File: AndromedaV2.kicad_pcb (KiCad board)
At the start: 2 copper layers, 100 x 65 mm, 94 parts, among them J1 USB_MINIB, J10 TEST_1P, J11 TEST_1P, J12 Micro_SD_Card, J13 TEST_1P, J14 TEST_1P, J15 TEST_1P, J16 TEST_1P, J17 TEST_1P, J18 GPS, J19 Radio, J2 TEST_1P, J20 Recovery, J21 Propulsion, J22 Tank Pressure, J23 Low Pressure, J24 Conn_01x06, J25 Battery, J26 Launch Systems, J27 SD, J3 TEST_1P, J4 TEST_1P, J5 TEST_1P, J6 TEST_1P, J7 TEST_1P, J8 TEST_1P, J9 TEST_1P, U1 FT230XS, U2 TPS562200, U3 AP2210-3.3, U4 AP2204K-5.0, U5 STM32F405R, U6 MS5607, U7 LSM9DS1, Y1 Crystal_8MHz_18pf

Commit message: further work on schematic and PCB
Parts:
- removed JP1, JP2: Jumper_NC_Small, Resistor_SMD:R_0603_1608Metric
- added C33: 0.1uF, Capacitors_SMD:C_0603, F.Cu at (166.6, 117.5)
- added C34: 0.5nF, Capacitors_SMD:C_0603, F.Cu at (171.3, 115.7)
- added C35: 1uF, Capacitors_SMD:C_0603, F.Cu at (164.1, 117.5)
- added R15: 330, Resistors_SMD:R_0603, F.Cu at (92.6, 108.5)
- added R16: 330, Resistors_SMD:R_0603, F.Cu at (92.6, 111.5)
- added R17: 30K, Resistors_SMD:R_0603, F.Cu at (134.4, 96.0)
- added R18: 10K, Resistors_SMD:R_0603, F.Cu at (134.4, 93.8)
- added R19: 13K, Resistors_SMD:R_0603, F.Cu at (164.7, 122.2)
- added R20: 200K, Resistors_SMD:R_0603, F.Cu at (169.7, 115.8)
- added R21: 100, Resistors_SMD:R_0603, F.Cu at (167.2, 115.3)
- added U8: INA326, Housings_SSOP:MSOP-8_3x3mm_Pitch0.65mm, F.Cu at (167.9, 121.7)
- C1, C10, C11, C12, C13, C14, C15, C16, C17, C18, C19, C2, C20, C21, C22, C23, C24, C25, C26, C27, C28, C29, C3, C30, C31, C32, C4, C5, C6, C7, C8, C9: footprint Capacitor_SMD:C_0603_1608Metric -> Capacitors_SMD:C_0603
- J10, J11, J13, J14, J15, J16, J17, J2, J3, J4, J5, J6, J7, J8, J9: footprint TestPoint:TestPoint_Pad_D2.0mm -> Connectors_TestPoints:Test_Point_Pad_d1.5mm
- MK1, MK2, MK3, MK4: value Mounting_Hole_PAD -> Mounting_Hole; footprint MountingHole:MountingHole_3.2mm_M3_Pad -> Mounting_Holes:MountingHole_3.2mm_M3
- R1, R10, R11, R12, R2, R3, R4, R5, R6, R7, R8, R9: footprint Resistor_SMD:R_0603_1608Metric -> Resistors_SMD:R_0603
- R13: value 330 -> 100K; footprint Resistor_SMD:R_0603_1608Metric -> Resistors_SMD:R_0603
- R14: value 330 -> 133K; footprint Resistor_SMD:R_0603_1608Metric -> Resistors_SMD:R_0603
- moved C30 91.8 mm to (108.0, 103.8)
- moved J7 77.7 mm to (177.8, 104.1)
- moved D2 76.6 mm to (97.5, 87.2), turned to 270 degrees
- moved D4 75.1 mm to (93.0, 92.2)
- moved C8 74.4 mm to (99.6, 80.3), turned to 90 degrees
- moved U6 72.4 mm to (102.3, 121.7)
- moved J15 71.8 mm to (107.0, 98.4)
- moved J9 71.3 mm to (104.2, 129.5)
- moved J27 66.7 mm to (185.6, 113.6)
- moved C12 63.9 mm to (91.6, 79.0), turned to 180 degrees
- moved C7 63.3 mm to (101.8, 80.3), turned to 90 degrees
- moved D3 62.9 mm to (96.1, 82.0)
- moved C22 62.9 mm to (115.9, 101.2), turned to 90 degrees
- moved C9 62.8 mm to (142.2, 94.4)
- moved C5 62.7 mm to (138.9, 82.7)
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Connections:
- net Baro_~CS renamed BARO_~CS
- J12 pad 2: SD_~CS -> SD1_~CS
- J13 pad 1: Net-(J13-Pad1) -> A/G_~CS
- J14 pad 1: Net-(J14-Pad1) -> SPI1_MOSI
- J15 pad 1: Net-(J15-Pad1) -> SPI1_SCK
- J18 pad 2: Net-(J18-Pad2) -> GND
- J18 pad 3: Net-(J18-Pad3) -> UART4_TX
- J18 pad 4: Net-(J18-Pad4) -> UART4_RX
- J19 pad 2: Net-(J19-Pad2) -> GND
- J19 pad 3: Net-(J19-Pad3) -> UART1_TX
- J19 pad 4: Net-(J19-Pad4) -> UART1_RX
- J20 pad 1: Net-(J20-Pad1) -> GND
- J20 pad 2: Net-(J20-Pad2) -> GND
- J20 pad 3: Net-(J20-Pad3) -> RECOVERY_2
- J20 pad 4: Net-(J20-Pad4) -> RECOVERY_1
- J21 pad 1: Net-(J21-Pad1) -> GND
- J21 pad 2: Net-(J21-Pad2) -> GND
- J21 pad 3: Net-(J21-Pad3) -> PROPULSION2
- J21 pad 4: Net-(J21-Pad4) -> PROPULSION1
- J22 pad 1: Net-(J22-Pad1) -> +5V
- J22 pad 2: Net-(J22-Pad2) -> GND
- J22 pad 3: Net-(J22-Pad3) -> GND
- J23 pad 2: Net-(J23-Pad2) -> GND
- J23 pad 3: Net-(J23-Pad3) -> GND
- J26 pad 1: Net-(J26-Pad1) -> LAUNCH
- J26 pad 2: Net-(J26-Pad2) -> UART2_TX
- J26 pad 3: Net-(J26-Pad3) -> UART2_RX
- J26 pad 5: Net-(J26-Pad5) -> GND
- J27 pad 1: Net-(J27-Pad1) -> +3V3
- J27 pad 2: Net-(J27-Pad2) -> GND
- J27 pad 3: Net-(J27-Pad3) -> SPI3_SCK
- J27 pad 4: Net-(J27-Pad4) -> SPI3_MOSI
- J27 pad 5: Net-(J27-Pad5) -> SPI3_MISO
- J27 pad 6: Net-(J27-Pad6) -> SD2_~CS
- J4 pad 1: SD_~CS -> SD1_~CS
- MK1 pad 1: GND -> (no net)
- MK2 pad 1: GND -> (no net)
- MK3 pad 1: GND -> (no net)
- MK4 pad 1: GND -> (no net)
- R10 pad 2: SD_~CS -> SD1_~CS
- R13 pad 1: LED1 -> Net-(J23-Pad4)
- R13 pad 2: Net-(D5-Pad2) -> ADC1
- R14 pad 1: LED2 -> ADC1
- R14 pad 2: Net-(D6-Pad2) -> GND
- U1 pad 1: Net-(JP1-Pad1) -> UART3_RX
- U1 pad 4: Net-(JP2-Pad1) -> UART3_TX
- U2 pad 5: Net-(U2-Pad5) -> Net-(R3-Pad2)
- U5 pad 11: Net-(U5-Pad11) -> LAUNCH
- U5 pad 14: Net-(U5-Pad14) -> UART4_TX
- U5 pad 15: Net-(U5-Pad15) -> UART4_RX
- U5 pad 16: Net-(U5-Pad16) -> UART2_TX
- U5 pad 17: MAG_~CS -> UART2_RX
- U5 pad 24: Net-(U5-Pad24) -> MAG_~CS
- U5 pad 25: Net-(U5-Pad25) -> LED1
- U5 pad 26: Net-(U5-Pad26) -> ADC1
- U5 pad 27: Net-(U5-Pad27) -> ADC2
- U5 pad 28: Net-(U5-Pad28) -> LED2
- U5 pad 29: Net-(U5-Pad29) -> UART3_TX
- U5 pad 30: Net-(U5-Pad30) -> UART3_RX
- U5 pad 38: Net-(U5-Pad38) -> RECOVERY_1
- U5 pad 39: Net-(U5-Pad39) -> RECOVERY_2
- U5 pad 44: Net-(U5-Pad44) -> PROPULSION1
- U5 pad 45: Net-(U5-Pad45) -> PROPULSION2
- U5 pad 50: Net-(U5-Pad50) -> SD1_~CS
- U5 pad 54: SD_~CS -> SD2_~CS
- U5 pad 58: Net-(U5-Pad58) -> UART1_TX
- U5 pad 59: Net-(U5-Pad59) -> UART1_RX
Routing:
- net GND: track 0.06 -> 435.7 mm, vias 0 -> 114
- net +3V3: track 0.00 -> 220.8 mm, vias 0 -> 10
- net ADC2: track 0.00 -> 64.1 mm, vias 0 -> 2
- net SD1_~CS: track 0.00 -> 60.2 mm, vias 0 -> 2
- net +BATT: track 2.87 -> 60.6 mm, vias 0 -> 7
- net UART4_RX: track 0.00 -> 54.6 mm, vias 0 -> 1
- net SD_~CS: track 53.6 -> 0.00 mm
- net UART4_TX: track 0.00 -> 50.4 mm, vias 0 -> 1
- net SD2_~CS: track 0.00 -> 48.4 mm, vias 0 -> 2
- net +5V: track 0.00 -> 47.6 mm, vias 0 -> 1
- net UART1_TX: track 0.00 -> 43.6 mm, vias 0 -> 2
- net UART1_RX: track 0.00 -> 41.9 mm, vias 0 -> 2
- net UART3_TX: track 0.00 -> 30.5 mm, vias 0 -> 2
- net ADC1: track 0.00 -> 30.4 mm, vias 0 -> 4
- net UART3_RX: track 0.00 -> 30.0 mm, vias 0 -> 2
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- added copper zone on B.Cu, net +3V3
- added copper zone on F.Cu, net +3V3
- added copper zone on B.Cu, net +BATT
- added copper zone on B.Cu, net GND
- added copper zone on F.Cu, net GND
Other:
- net class Default: clearance 0.2 -> 0.15
- rule trace_clearance: 0.2 -> 0.15
- rule trace_min: 0.2 -> 0.18

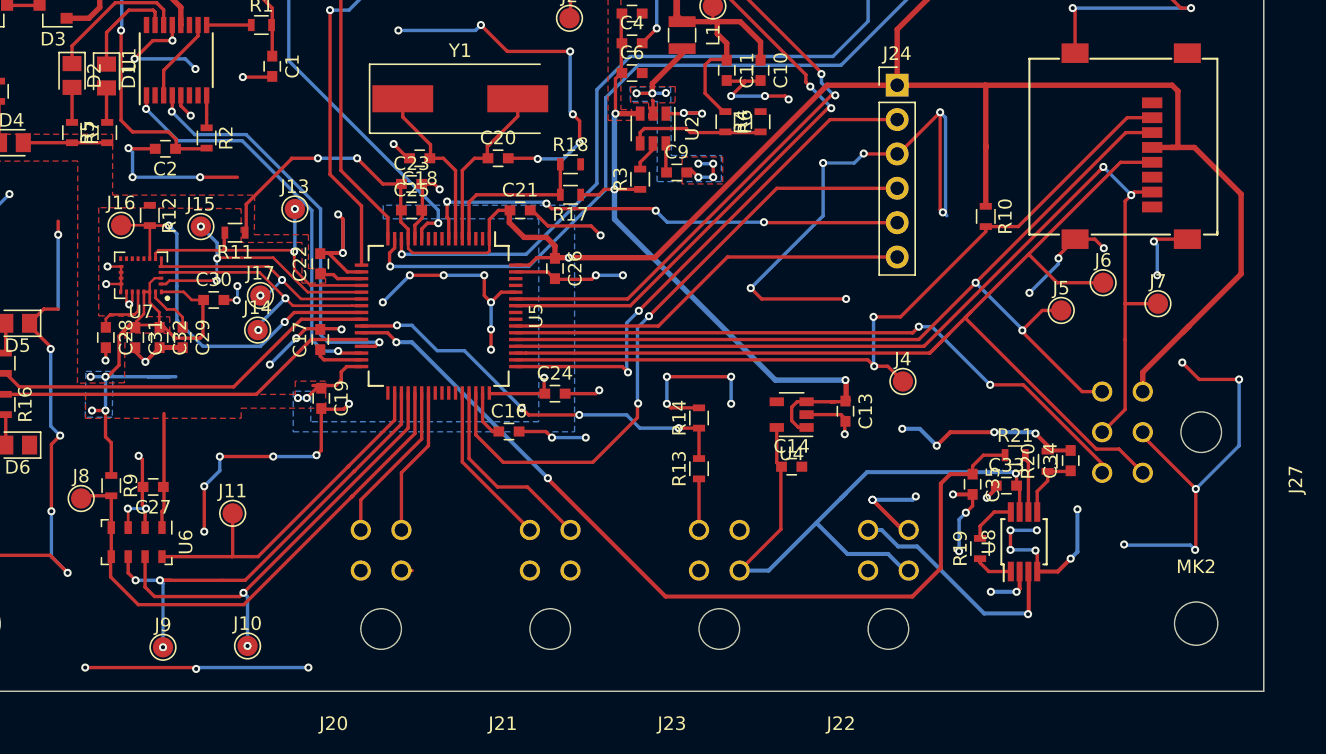
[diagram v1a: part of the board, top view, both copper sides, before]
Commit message: Bring schematic in line with PCB. Previous update broke this.
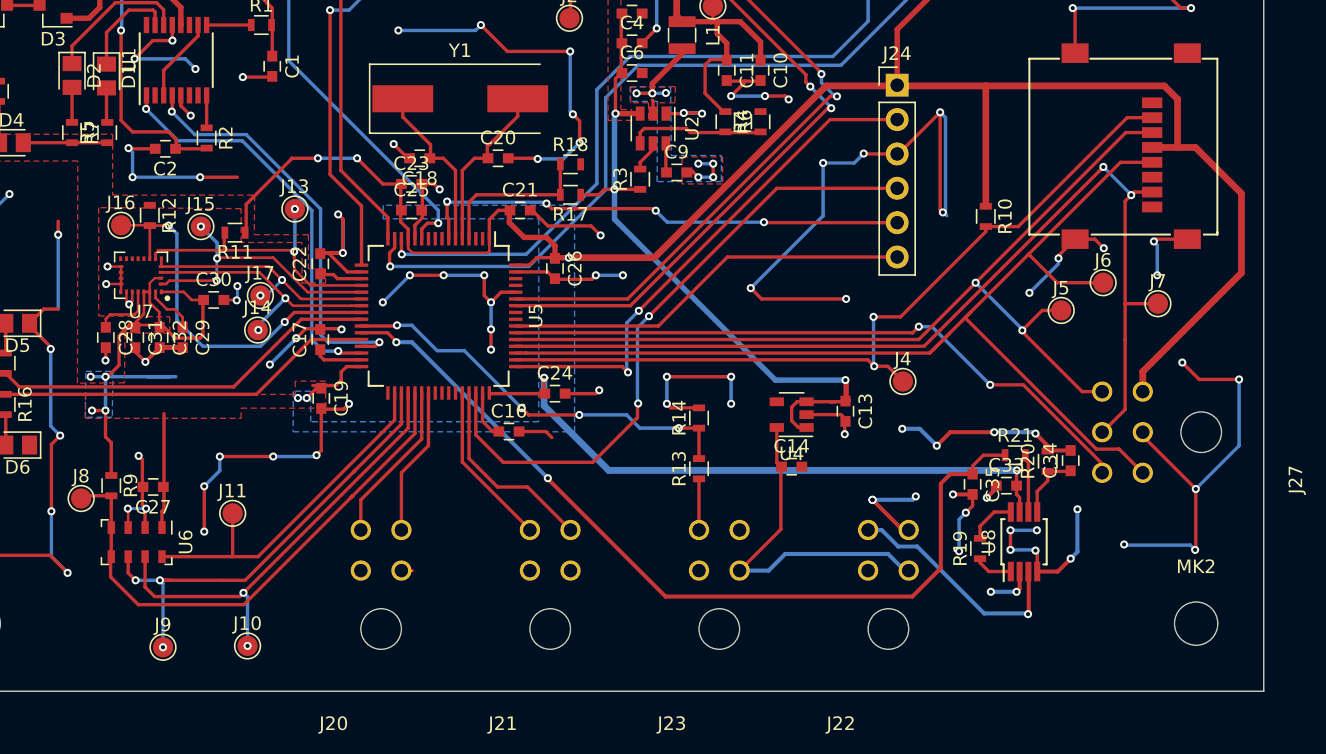
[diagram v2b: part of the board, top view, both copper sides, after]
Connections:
- C33 pad 2: +5V -> +3V3
- U8 pad 7: +5V -> +3V3
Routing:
- net +3V3: track 220.8 -> 261.3 mm, vias 10 -> 11
- net +5V: track 47.6 -> 25.5 mm, vias 1 -> 0
- net (no net): track 23.1 -> 6.50 mm, vias 4 -> 1
- net GND: track 435.7 -> 433.2 mm, vias 114 -> 112

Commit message: Changes based on review reccommemdations
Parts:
- added C36: 10u, Capacitors_SMD:C_0603, F.Cu at (180.8, 104.4)
- added C37: 10u, Capacitors_SMD:C_0603, F.Cu at (166.2, 84.8)
- added D7: D_TVS, Diodes_SMD:D_SOD-323, F.Cu at (126.5, 82.6)
- added R22: 10K, Resistors_SMD:R_0603, F.Cu at (162.5, 111.3)
- moved R4 0.83 mm to (147.6, 90.6)
- moved R6 0.45 mm to (145.4, 90.6)
- moved C26 0.40 mm to (133.2, 101.9)
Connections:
- R5 pad 1: +3V3 -> Net-(R5-Pad1)
- R7 pad 2: +3V3 -> Net-(R5-Pad1)
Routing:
- net +3V3: track 261.3 -> 267.4 mm, vias 11 -> 13
- net GND: track 433.2 -> 430.6 mm, vias 112 -> 110
- net SD2_~CS: track 48.4 -> 51.0 mm
- net Net-(R5-Pad1): track 0.00 -> 2.60 mm
- net +12V: track 9.75 -> 11.5 mm
- net Net-(R4-Pad1): track 9.95 -> 9.11 mm
- net UART1_RX: track 42.1 -> 42.7 mm
- net UART1_TX: track 43.6 -> 44.1 mm
- net (no net): vias 1 -> 3

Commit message: Final design published. Gerbers and PDF schematic generated
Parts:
- added J28: Conn_01x02, SOAR_Kicad_Library:TerminalBlock_5mm_2POS_ED2600, F.Cu at (173.1, 74.6)
- added LOGO_SOAR: , SOAR_Kicad_Library:LOGO_SOAR, F.Cu at (144.1, 97.4)
- added Q1: Q_NMOS_GSD, TO_SOT_Packages_SMD:SOT-23, F.Cu at (176.0, 81.5)
- J1: footprint SOAR_Library:USB-Mini-B -> SOAR_Kicad_Library:USB-Mini-B
- J12: footprint SOAR_Library:Conn,Molex,Hinged_microSD -> SOAR_Kicad_Library:Conn,Molex,Hinged_microSD
- J18, J19, J20, J21, J22, J23, J25: footprint SOAR_Library:Molex_Micro-Fit_3.0_43045-0400_2x02_P3.00mm_Horizontal -> SOAR_Kicad_Library:Molex_Micro-Fit_3.0_43045-0400_2x02_P3.00mm_Horizontal
- J26, J27: footprint SOAR_Library:Molex_Micro-Fit_3.0_43045-0600_2x03_P3.00mm_Horizontal -> SOAR_Kicad_Library:Molex_Micro-Fit_3.0_43045-0600_2x03_P3.00mm_Horizontal
- L1: value L -> 4.7uH; footprint SOAR_Library:L_1008 -> SOAR_Kicad_Library:L_1008
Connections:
- U5 pad 57: Net-(U5-Pad57) -> Fan_ctrl
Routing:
- net GND: track 430.6 -> 738.7 mm, vias 110 -> 149
- net Fan_ctrl: track 0.00 -> 65.1 mm, vias 0 -> 2
- net +5VP: track 25.1 -> 59.4 mm
- net Net-(J28-Pad1): track 0.00 -> 7.62 mm
- net (no net): track 6.50 -> 0.00 mm, vias 3 -> 2
- net Net-(C20-Pad1): track 12.7 -> 12.1 mm
- net Net-(C18-Pad1): track 12.5 -> 12.0 mm
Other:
- board text added: "3V3"
- board text added: "Andromeda Sensor Board V2 (May 2018)"
- board text added: "Battery"
- board text added: "GND"
- board text added: "GPS"
- board text added: "Launch"
- board text added: "Propulsion"
- board text added: "Radio"
- board text added: "Recovery"
- board text added: "SD Card"
- board text added: "SWCLK"
- board text added: "SWDIO"
- board text added: "SWO"
- board text added: "Tank"
- board text added: "Vent"
- board text added: "~RST"
